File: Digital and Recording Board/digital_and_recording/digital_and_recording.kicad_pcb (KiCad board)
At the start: 4 copper layers, 47 x 89.5 mm, 32 parts, among them J1 Headphones, J2 Screen, J3 USB_Breakout, J4 Joystick, J5 Conn_02x20_Odd_Even, U1 Daisy_Seed, U2 Daisy_Seed_Recording, U3 Bypass 2, U4 Bypass 1, U5 Output Select

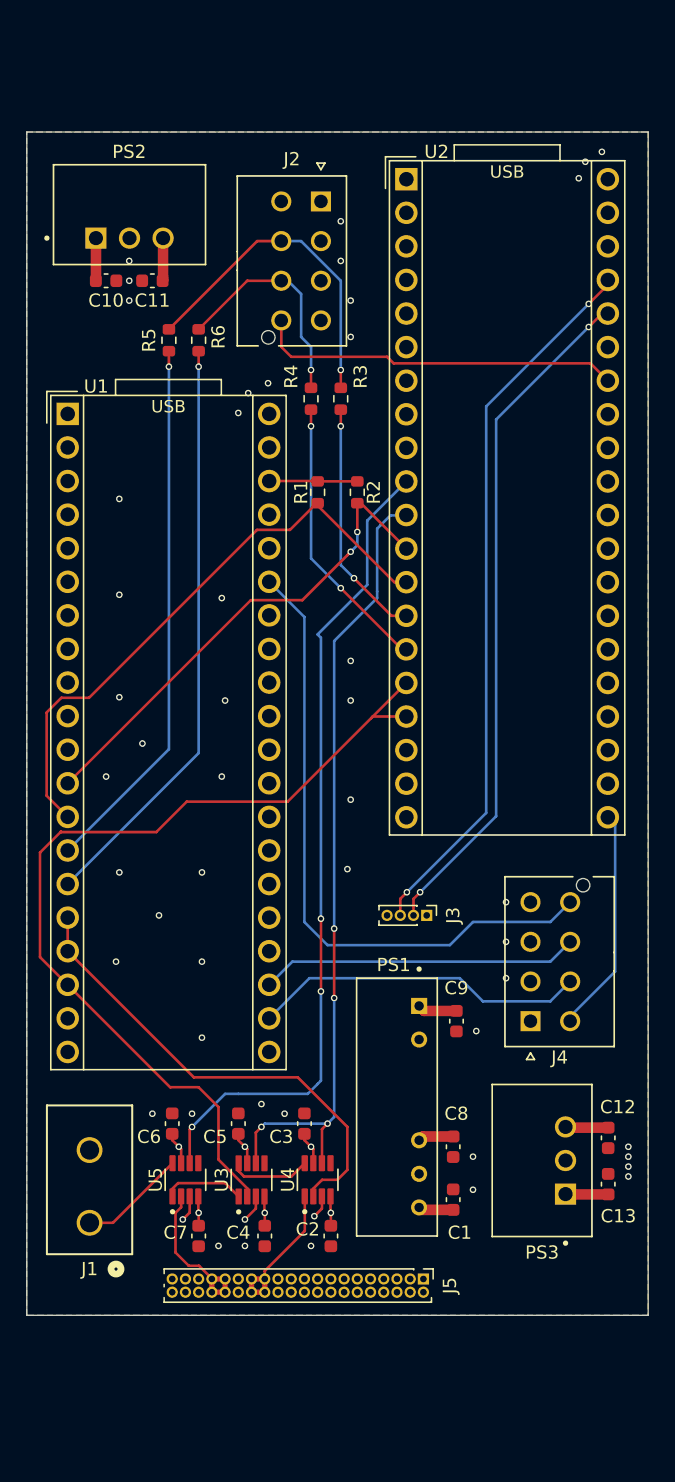
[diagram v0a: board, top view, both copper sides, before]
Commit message: added fun silk screens
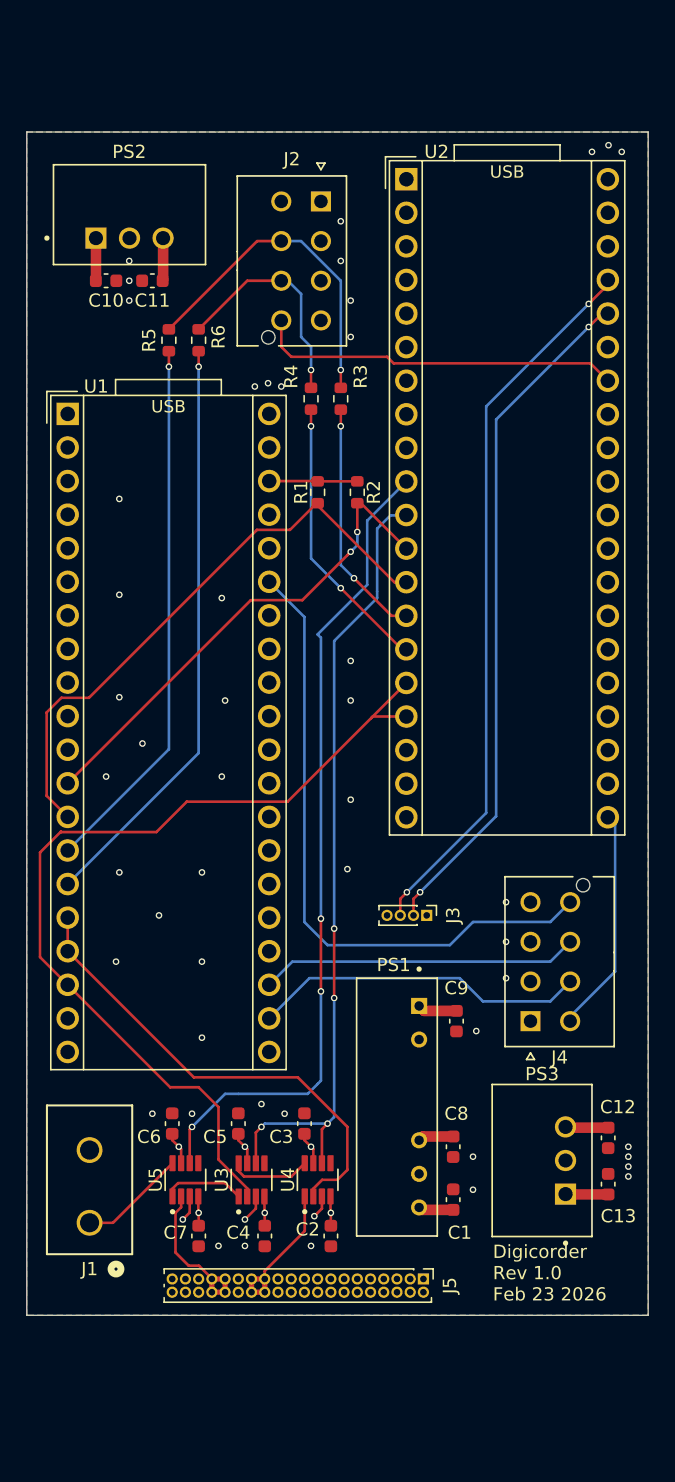
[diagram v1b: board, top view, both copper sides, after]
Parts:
- added G***: LOGO, LOGO, B.Cu at (166.8, 106.8)
- added G***: LOGO, LOGO, B.Cu at (137.1, 121.0)
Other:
- board text added: "Digicorder Rev 1.0 Feb 23 2026"
- board text added: "{dblquote}I actually do know a girl named Speaker{dblquote} - Marco Yaipen"
- board text added: "{dblquote}Speaker...? I barely know her{dblquote} - Kyle de Nobel"

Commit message: corrected connectors
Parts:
- removed J5: Conn_02x20_Odd_Even, Connector_PinHeader_1.00mm:PinHeader_2x20_P1.00mm_Vertical
- added H1: MountingHole, MountingHole:MountingHole_2.7mm_M2.5, F.Cu at (171.6, 51.2)
- added H2: MountingHole, MountingHole:MountingHole_2.7mm_M2.5, F.Cu at (130.4, 51.2)
- added H3: MountingHole, MountingHole:MountingHole_2.7mm_M2.5, F.Cu at (130.4, 151.6)
- added H4: MountingHole, MountingHole:MountingHole_2.7mm_M2.5, F.Cu at (171.6, 151.6)
- added J6: MINIFIT-2-VERT, Connector_Molex:Molex_Mini-Fit_Jr_5566-02A_2x01_P4.20mm_Vertical, F.Cu at (153.5, 143.8)
- added J7: MINIFIT-2-VERT, Connector_Molex:Molex_Mini-Fit_Jr_5566-02A_2x01_P4.20mm_Vertical, F.Cu at (132.5, 143.8)
- added J8: MINIFIT-2-VERT, Connector_Molex:Molex_Mega-Fit_76829-0102_2x01_P5.70mm_Vertical, F.Cu at (162.8, 143.8)
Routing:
- net /Connectors/Guitar_Out: track 12.0 -> 9.23 mm
- net /Connectors/Guitar_In: track 11.5 -> 8.96 mm
- added copper zone on In2.Cu, net GND
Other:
- board size 47 x 89.5 mm -> 47 x 106.3 mm
